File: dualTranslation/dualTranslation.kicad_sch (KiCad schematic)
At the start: 17 parts, among them IC1 LSF0108PWR, IC2 LSF0108PWR, J1 L_dual, J2 R_dual, J6 MISC

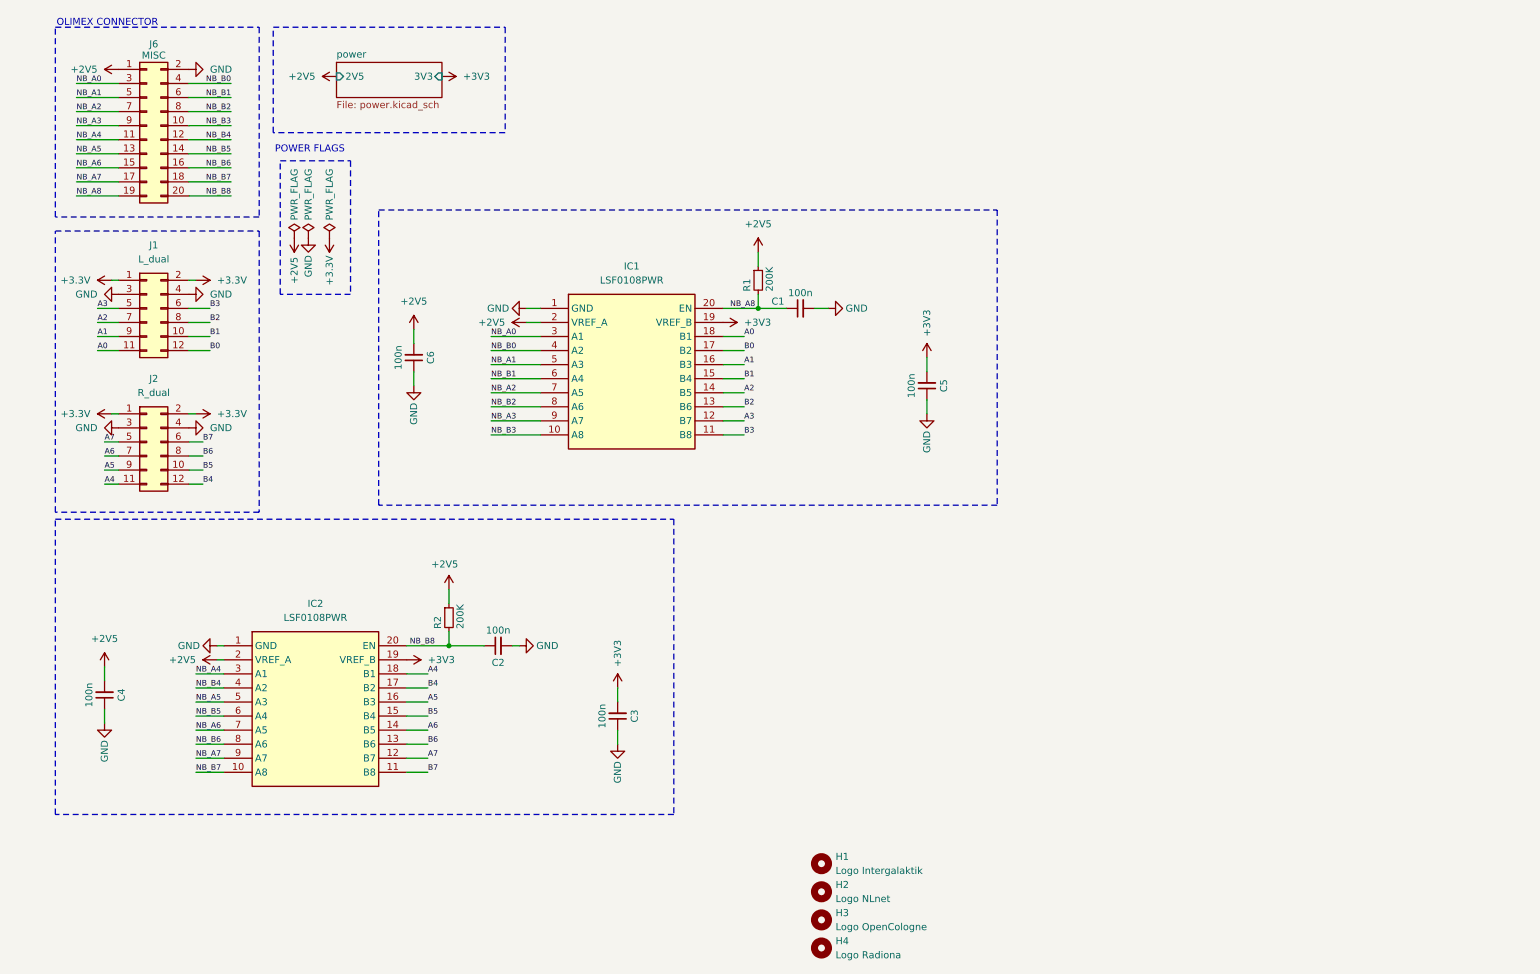
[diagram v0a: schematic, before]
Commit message: Adding PULL UPs on LOW Level
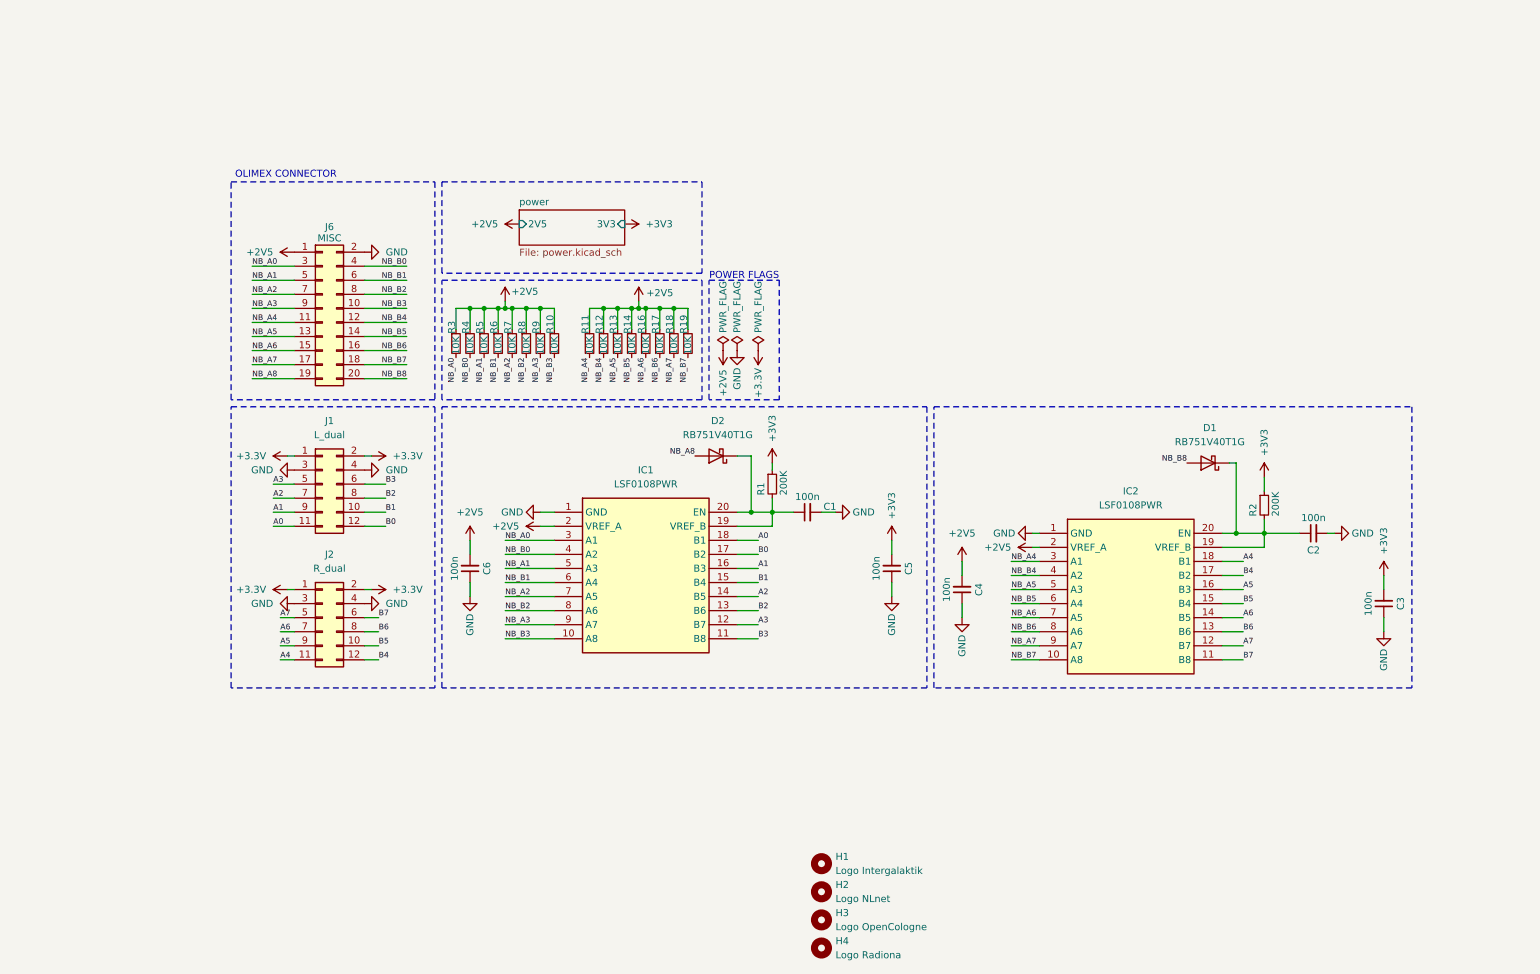
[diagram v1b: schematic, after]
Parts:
- added D1, D2: RB751V40T1G, symbol Device:D_Schottky
- added R10, R11, R12, R13, R14, R16, R17, R18, R19, R3, R4, R5, R6, R7, R8, R9: 10K, Resistor_SMD:R_0402_1005Metric, symbol Device:R_Small
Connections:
- net +2V5: now also R10.1, R11.1, R12.1, R13.1, R14.1, R16.1, R17.1, R18.1, R19.1, R3.1, R4.1, R5.1, R6.1, R7.1, R8.1, R9.1; no longer R1.1, R2.1
- net +3V3: now also R1.1, R2.1; no longer IC1.19 (VREF_B), IC2.19 (VREF_B)
- net NB_A0: now also R3.2
- net NB_A1: now also R5.2
- net NB_A2: now also R7.2
- net NB_A3: now also R9.2
- net NB_A4: now also R11.2
- net NB_A5: now also R13.2
- net NB_A6: now also R16.2
- net NB_A7: now also R18.2
- net NB_A8: now also D2.2 (A); no longer C1.1, IC1.20 (EN), R1.2
- net NB_B0: now also R4.2
- net NB_B1: now also R6.2
- net NB_B2: now also R8.2
- net NB_B3: now also R10.2
- net NB_B4: now also R12.2
- net NB_B5: now also R14.2
- net NB_B6: now also R17.2
- net NB_B7: now also R19.2
- net NB_B8: now also D1.2 (A); no longer C2.1, IC2.20 (EN), R2.2
- new net: C1.1, D2.1 (K), IC1.19 (VREF_B), IC1.20 (EN), R1.2
- new net: C2.1, D1.1 (K), IC2.19 (VREF_B), IC2.20 (EN), R2.2
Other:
- company: (none) -> Intergalaktik d.o.o.
- title: (none) -> Dual Translation
- moved on the sheet: C1, C2, C3, C4, C5, C6, IC1, IC2, J1, J2, J6, R1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

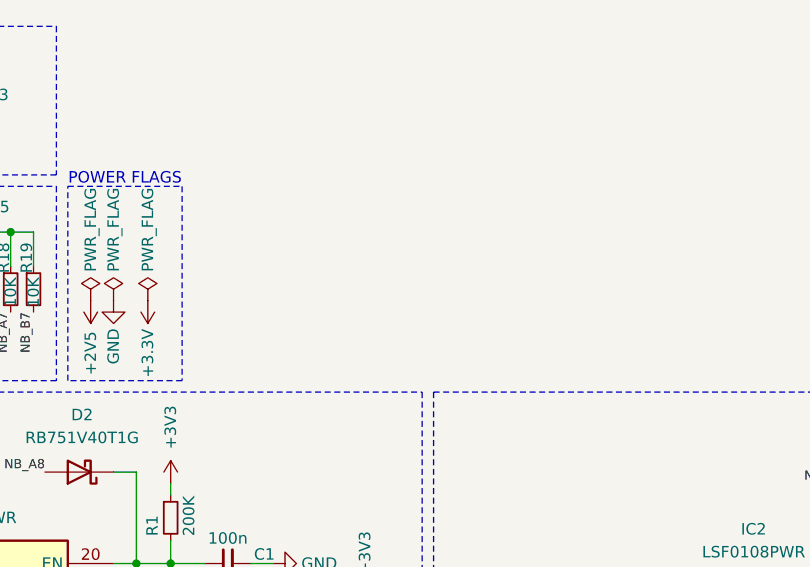
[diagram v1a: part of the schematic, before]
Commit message: Adding PULL UPs on HIGH Level
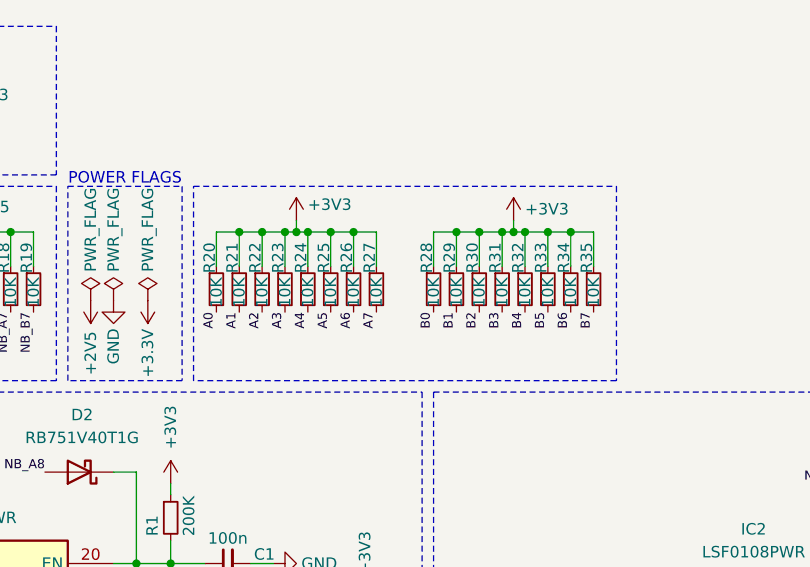
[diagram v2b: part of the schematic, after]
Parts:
- added R20, R21, R22, R23, R24, R25, R26, R27, R28, R29, R30, R31, R32, R33, R34, R35: 10K, Resistor_SMD:R_0402_1005Metric, symbol Device:R_Small
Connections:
- net +3V3: now also R20.1, R21.1, R22.1, R23.1, R24.1, R25.1, R26.1, R27.1, R28.1, R29.1, R30.1, R31.1, R32.1, R33.1, R34.1, R35.1
- net A0: now also R20.2
- net A1: now also R21.2
- net A2: now also R22.2
- net A3: now also R23.2
- net A4: now also R24.2
- net A5: now also R25.2
- net A6: now also R26.2
- net A7: now also R27.2
- net B0: now also R28.2
- net B1: now also R29.2
- net B2: now also R30.2
- net B3: now also R31.2
- net B4: now also R32.2
- net B5: now also R33.2
- net B6: now also R34.2
- net B7: now also R35.2

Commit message: Adding diode footprint
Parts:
- D1, D2: footprint (none) -> Diode_SMD:D_SOD-323
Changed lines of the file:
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@@
 			)
 		)
-		(property "Footprint" ""
+		(property "Footprint" "Diode_SMD:D_SOD-323"
 			(at 135.89 93.98 0)
 			(effects
@@
 			)
 		)
-		(property "Footprint" ""
+		(property "Footprint" "Diode_SMD:D_SOD-323"
 			(at 224.79 95.25 0)
 			(effects

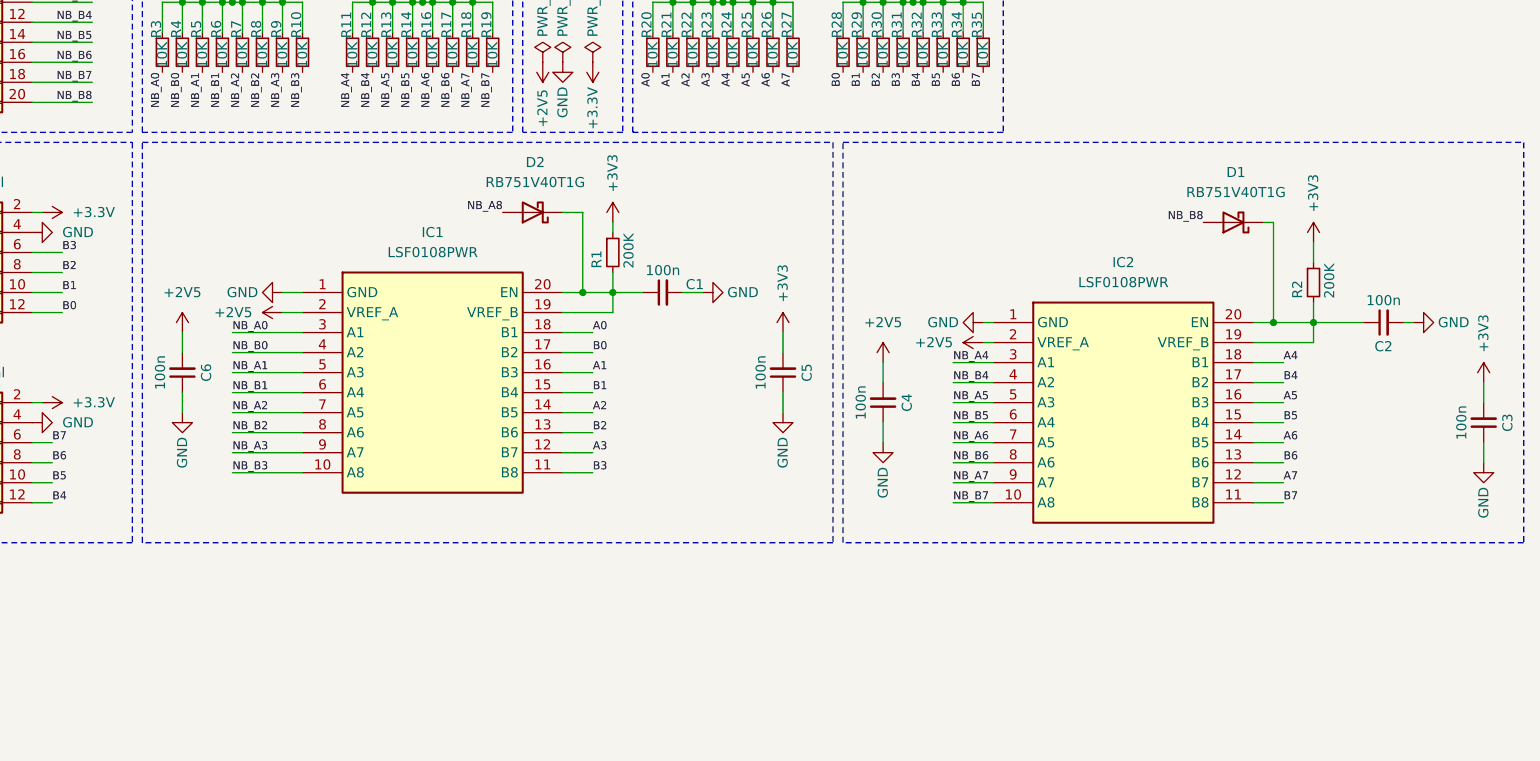
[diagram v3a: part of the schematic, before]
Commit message: Adding transistor
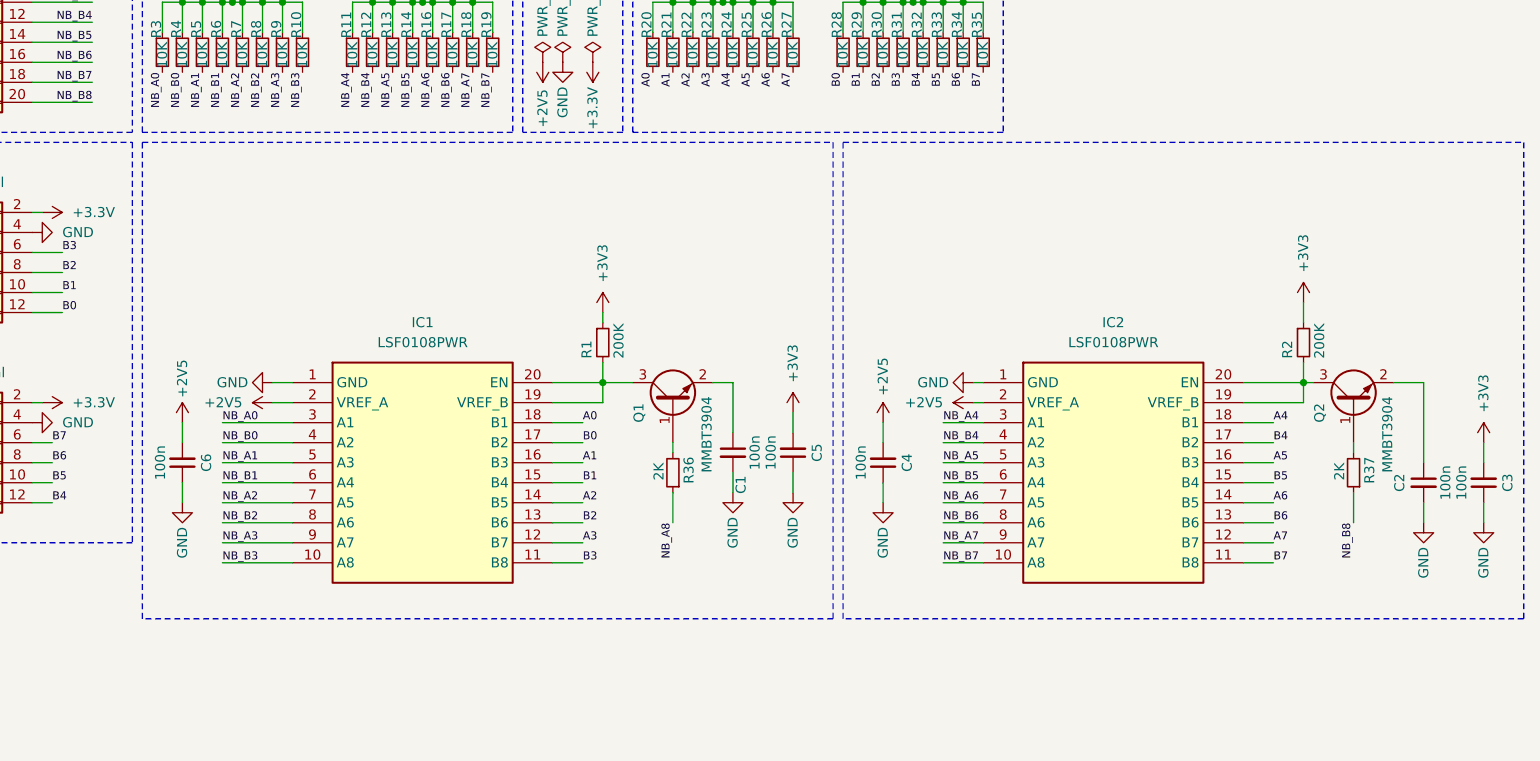
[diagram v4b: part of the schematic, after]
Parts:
- removed D1, D2: RB751V40T1G, Diode_SMD:D_SOD-323, symbol Device:D_Schottky
- added Q1, Q2: MMBT3904, Package_TO_SOT_SMD:SOT-23, symbol Transistor_BJT:MMBT3904
- added R36, R37: 2K, Resistor_SMD:R_0402_1005Metric, symbol Device:R_Small
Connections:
- net NB_A8: now also R36.1
- net NB_B8: now also R37.1
- net at IC1.19 (VREF_B), IC1.20 (EN), R1.2: now also Q1.3 (C); no longer C1.1
- net at IC2.19 (VREF_B), IC2.20 (EN), R2.2: now also Q2.3 (C); no longer C2.1
- new net: C1.1, Q1.2 (E)
- new net: Q2.1 (B), R37.2
- new net: C2.1, Q2.2 (E)
- new net: Q1.1 (B), R36.2
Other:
- moved on the sheet: C1, C2, C3, C4, C5, C6, IC1, IC2, R1, R2

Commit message: Routing
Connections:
- net GND: now also C2.1, Q1.2 (E), Q2.2 (E); no longer C2.2
- net at IC1.19 (VREF_B), IC1.20 (EN), Q1.3 (C)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: now also C1.1
- net at IC2.19 (VREF_B), IC2.20 (EN), Q2.3 (C)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: now also C2.2
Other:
- moved on the sheet: C1, C2, C3, C4, C5, IC2, Q1, Q2, R2, R36, R37

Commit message: moving to v9
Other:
- note added: "${project_creator} License: ${project_license} Year: ${project_year}"
- note added: "......"
- note added: "1"
- note added: "2"
- note added: "BOTTOM VIEW"
- note added: "CoverPage"
- note added: "Dual translation"
- note added: "Index"
- note added: "Page"
- note added: "Power"
- note added: "TOP VIEW"
- company: Intergalaktik d.o.o. -> ${project_creator}
- title: Dual Translation -> ${project_name} ${project_version}
- moved on the sheet: C1, C2, C3, C4, C5, C6, IC1, IC2, J1, J2, J6, Q1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

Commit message: Fix #5
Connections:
- net +3.3V is gone; now on net +3V3: J1.1 (Pin_1), J1.2 (Pin_2), J2.1 (Pin_1), J2.2 (Pin_2)
